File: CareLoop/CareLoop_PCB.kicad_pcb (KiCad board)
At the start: 6 copper layers, 39 x 23 mm, 74 parts, among them J1 Conn_Coaxial_Small, J1_Battery1 Conn_01x02_Pin, J1_DEBUG1 Conn_01x04_Pin, J2 USB_B_Micro, U1 MCP1700x-180xxMB, U2 MAX30102, U3 MPU-6050, U4 MCP1700x-330xxMB, U5 TP4056-42-ESOP8, U6 nRF52840-QFXX, U7 PCA9306, Y1 32MHz, Y2 32.768kHz

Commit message: PCB update
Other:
- board text added: "+"
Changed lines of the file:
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@@
 		(layer "Edge.Cuts")
+	)
+	(gr_text "+"
+		(at 132.35 88.9 0)
+		(layer "F.SilkS")
+		(effects
+			(font
+				(size 1.5 1.5)
+				(thickness 0.3)
+				(bold yes)
+			)
+			(justify left bottom)
+		)
 	)
 	(gr_text "CareLoop_V1.0"

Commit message: update PCB
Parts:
- removed J1: Conn_Coaxial_Small, Connector_Coaxial:U.FL_Molex_MCRF_73412-0110_Vertical
- L1, L2: footprint Inductor_SMD:L_0402_1005Metric_Pad0.77x0.64mm_HandSolder -> Inductor_SMD:L_0201_0603Metric_Pad0.64x0.40mm_HandSolder
- moved C43 0.85 mm to (129.9, 99.1)
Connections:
- C50 pad 1: Net-(J1-Ext) -> /Antenna/ANT
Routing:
- net Net-(J1-Ext): track 10.3 -> 0.00 mm
- net /Antenna/ANT: track 1.53 -> 9.05 mm
- net /Battery/VCC: track 20.6 -> 14.9 mm
- net /MAX30102/SDA: track 25.6 -> 23.5 mm
- net GND: vias 88 -> 94

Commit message: update PCB
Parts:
- J1_Battery1, JP1_MAX30102, JP2_MPU1, JP2_MPU2: footprint Connector_PinHeader_1.00mm:PinHeader_1x02_P1.00mm_Vertical -> Connector_PinHeader_2.00mm:PinHeader_1x02_P2.00mm_Vertical
- J1_DEBUG1: footprint Connector_PinHeader_1.00mm:PinHeader_1x04_P1.00mm_Vertical -> Connector_PinHeader_2.00mm:PinHeader_1x04_P2.00mm_Vertical
- moved JP2_MPU1 8.44 mm to (126.2, 101.2), turned to 90 degrees
- moved J1_DEBUG1 4.25 mm to (153.4, 105.8)
- moved R41 1.95 mm to (128.1, 91.3)
- moved C40 1.95 mm to (125.6, 92.3)
- moved C41 1.95 mm to (125.6, 91.3)
- moved C42 1.95 mm to (125.5, 96.5)
- moved D41 1.95 mm to (127.5, 89.7)
- moved C43 1.95 mm to (128.0, 99.1)
- moved D40 1.95 mm to (126.2, 89.7)
- moved U4 1.95 mm to (126.5, 98.0)
- moved U5 1.95 mm to (126.9, 91.6)
- moved R40 1.90 mm to (128.8, 89.7)
- moved R42 1.90 mm to (126.9, 94.0)
- moved JP2_MPU2 1.64 mm to (130.9, 93.5)
- moved J1_Battery1 1.10 mm to (131.5, 90.5)
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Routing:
- net /Battery/BAT_Plus: track 20.4 -> 28.7 mm
- net /Battery/VCC: track 14.9 -> 18.8 mm, vias 14 -> 13
- net /MCU/SWDIO: track 4.81 -> 7.75 mm
- net /Battery/VBUS: track 20.4 -> 23.1 mm
- net /MCU/SWDCLK: track 4.23 -> 6.24 mm
- net /MPU6050/VIN_MPU: track 13.4 -> 15.1 mm
- net /Battery/VIN_BATTERY: track 8.76 -> 7.58 mm
- net GND: track 10.5 -> 11.4 mm, vias 94 -> 92
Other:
- board size 39 x 23 mm -> 41.1 x 23 mm

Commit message: nordic review
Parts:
- moved C9 1.12 mm to (154.1, 95.4)
- moved C7 1.12 mm to (152.1, 95.3)
- moved C5 0.84 mm to (150.7, 95.8), turned to 90 degrees
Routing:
- net /MCU/DEC3: track 3.69 -> 5.38 mm, vias 1 -> 2
- net GND: track 11.4 -> 13.0 mm, vias 92 -> 120
- net /MCU/DEC4/DEC6: vias 3 -> 4

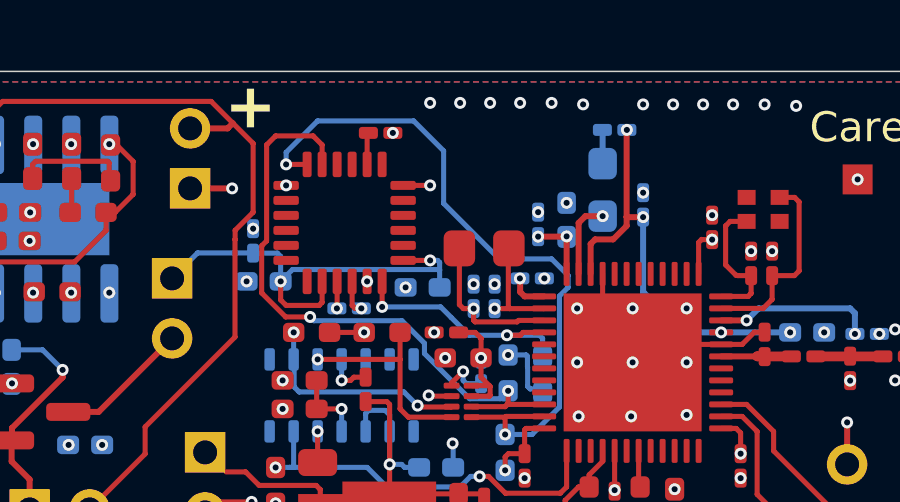
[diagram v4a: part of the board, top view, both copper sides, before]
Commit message: update Voltagedevider
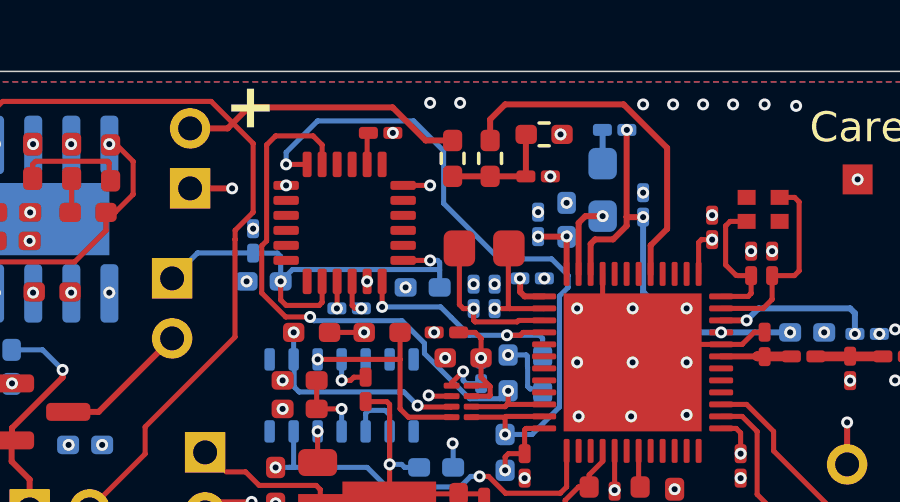
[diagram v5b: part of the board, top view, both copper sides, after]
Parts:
- added C13: 100n, Capacitor_SMD:C_0201_0603Metric_Pad0.64x0.40mm_HandSolder, F.Cu at (143.1, 90.2)
- added R43: 120k, Resistor_SMD:R_0402_1005Metric_Pad0.72x0.64mm_HandSolder, F.Cu at (140.2, 89.5)
- added R44: 100, Resistor_SMD:R_0402_1005Metric_Pad0.72x0.64mm_HandSolder, F.Cu at (141.5, 89.5)
- added R45: 300k, Resistor_SMD:R_0402_1005Metric_Pad0.72x0.64mm_HandSolder, F.Cu at (143.3, 88.8)
- C10: value 100p -> 100n
- C3, C4: value 12p -> 4p
- R4: value 300 -> 800
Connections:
- U6 pad 41: unconnected-(U6-P0.28-Pad41) -> /Battery/Vin_Battery_Status
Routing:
- net /Battery/Vin_Battery_Status: track 0.00 -> 11.8 mm
- net /Battery/BAT_Plus: track 28.7 -> 36.7 mm
- net Net-(C13-Pad2): track 0.00 -> 3.80 mm
- net GND: vias 120 -> 118
